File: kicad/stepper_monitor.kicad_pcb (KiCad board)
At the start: 2 copper layers, 38.5 x 43 mm, 58 parts, among them J1 Conn_01x04_Pin, J2 Conn_01x04_Pin, J3 Conn_01x02_Pin, J4 USB_C_Receptacle_USB2.0, J5 JTAG, Q1 MMDT2222A, SW1 SW_Push, U1 5V, U2 CP2102N-A01-GQFN28, U3 AMS1117-3.3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

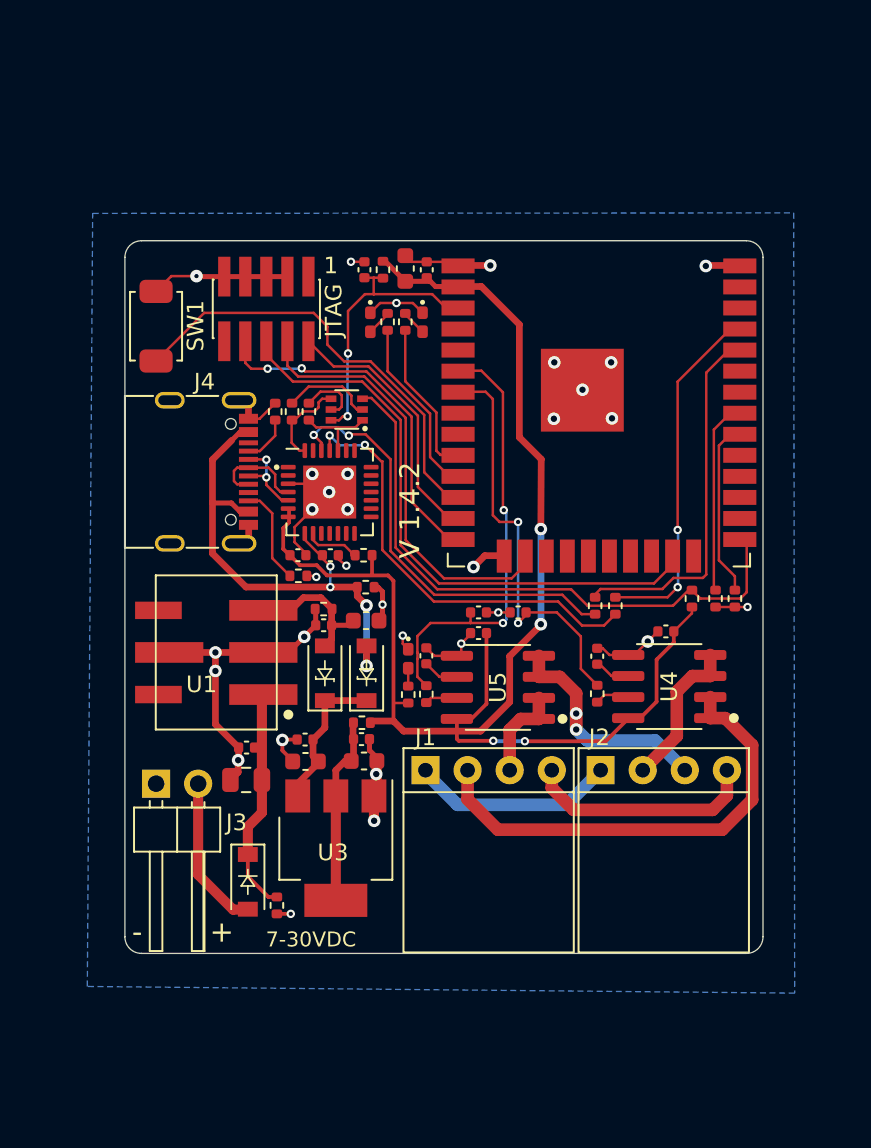
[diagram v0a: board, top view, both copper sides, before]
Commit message: V3D Edition Design
- M3 corner holes
- JST XH connectors
- Match JLCPCB capabilities
- increased board size
- increased via size
- adjusted tracks in some locations to match capabilities
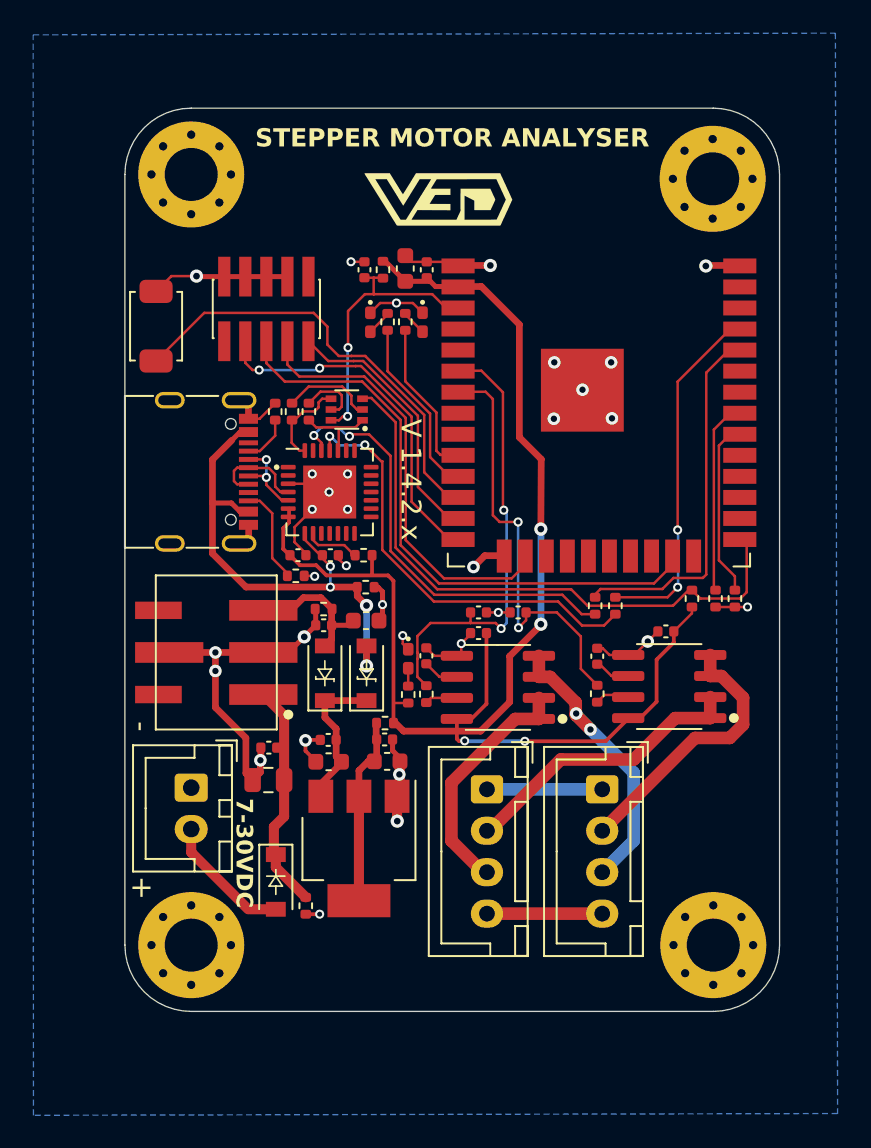
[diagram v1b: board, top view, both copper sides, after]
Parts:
- added G***: LOGO, LOGO, F.Cu at (18.9, -45.5)
- added H1: MountingHole, MountingHole:MountingHole_3.2mm_M3_Pad_Via, F.Cu at (4.00, -47.0)
- added H2: MountingHole, MountingHole:MountingHole_3.2mm_M3_Pad_Via, F.Cu at (35.5, -46.7)
- added H3: MountingHole, MountingHole:MountingHole_3.2mm_M3_Pad_Via, F.Cu at (4.00, -0.50)
- added H4: MountingHole, MountingHole:MountingHole_3.2mm_M3_Pad_Via, F.Cu at (35.5, -0.50)
- J1, J2: footprint stepper_monitor:connector_4pins_horizontal -> Connector_JST:JST_XH_B4B-XH-A_1x04_P2.50mm_Vertical
- J3: footprint stepper_monitor:PinHeader_1x02_P2.54mm_Horizontal_JLCPCB -> Connector_JST:JST_XH_B2B-XH-A_1x02_P2.50mm_Vertical
- moved J2 3.89 mm to (28.8, -9.90), turned to -90 degrees
- moved R3 1.74 mm to (10.9, -2.87)
- moved D3 1.69 mm to (9.11, -4.31)
- moved C10 1.39 mm to (15.8, -11.6)
- moved C11 1.39 mm to (15.7, -12.9)
- moved C6 1.39 mm to (12.3, -11.6)
- moved C8 1.39 mm to (12.3, -12.9)
- moved R16 1.39 mm to (15.7, -13.9)
- moved U3 1.39 mm to (14.1, -6.33)
- moved C2 1.34 mm to (8.68, -12.4)
- moved C1 1.34 mm to (8.66, -10.5)
- moved J1 1.16 mm to (21.8, -9.90), turned to -90 degrees
- moved J3 0.88 mm to (4.00, -10.0), turned to -90 degrees
- moved R5 0.15 mm to (10.3, -22.8)
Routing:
- net Net-(J1-Pin_2): track 28.2 -> 16.8 mm
- net Net-(J1-Pin_3): track 5.74 -> 14.6 mm
- net Net-(J2-Pin_2): track 9.27 -> 16.6 mm
- net Net-(J1-Pin_4): track 14.1 -> 6.96 mm
- net Net-(J1-Pin_1): track 12.4 -> 6.96 mm
- net Net-(J2-Pin_3): track 14.6 -> 17.9 mm
- net GNDD: track 77.7 -> 79.9 mm
- net Net-(D3-A): track 9.46 -> 7.81 mm
- net +3V3: track 91.2 -> 89.8 mm
- net CHB: track 25.2 -> 25.8 mm
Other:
- board size 38.5 x 43 mm -> 39.5 x 54.5 mm
- board text added: "ESP32,OSH,github/zapta"
- board text added: "JLCJLCJLCJLC"
- board text added: "STEPPER MOTOR ANALYSER"
- board text added: "V 1.4.2.x"
- board text removed: "1"
- board text removed: "STEPPER MOTOR ANALYZER ESP32, OSH, github/zapta"
- board text removed: "V 1.4.2"
